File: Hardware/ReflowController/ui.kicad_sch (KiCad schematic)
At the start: 46 parts, among them J601 LCD_HEADER, Q601 BC848, SW601 RotaryEncoder_Switch, SW602 SW_UP, SW603 SW_DOWN, SW604 SW_LEFT, SW605 SW_RIGHT, SW606 SW_SELECT, SW607 SW_RET, SW608 SW_RESET, U601 PI4IOE5V6416

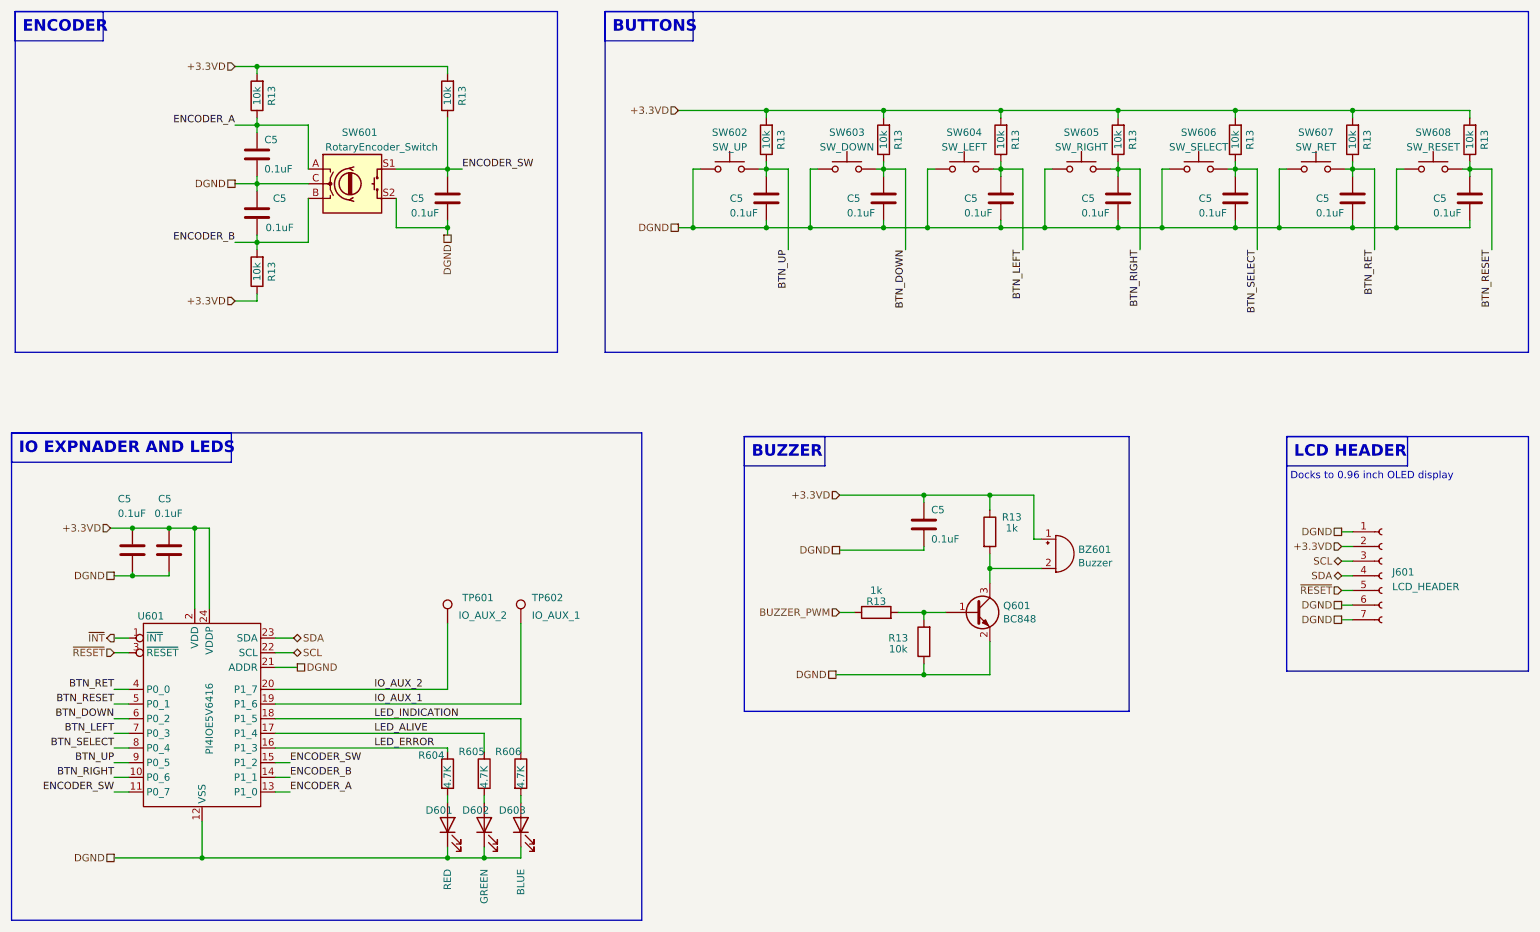
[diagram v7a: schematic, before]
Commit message: Advancing on the pcb removed netties from MCU
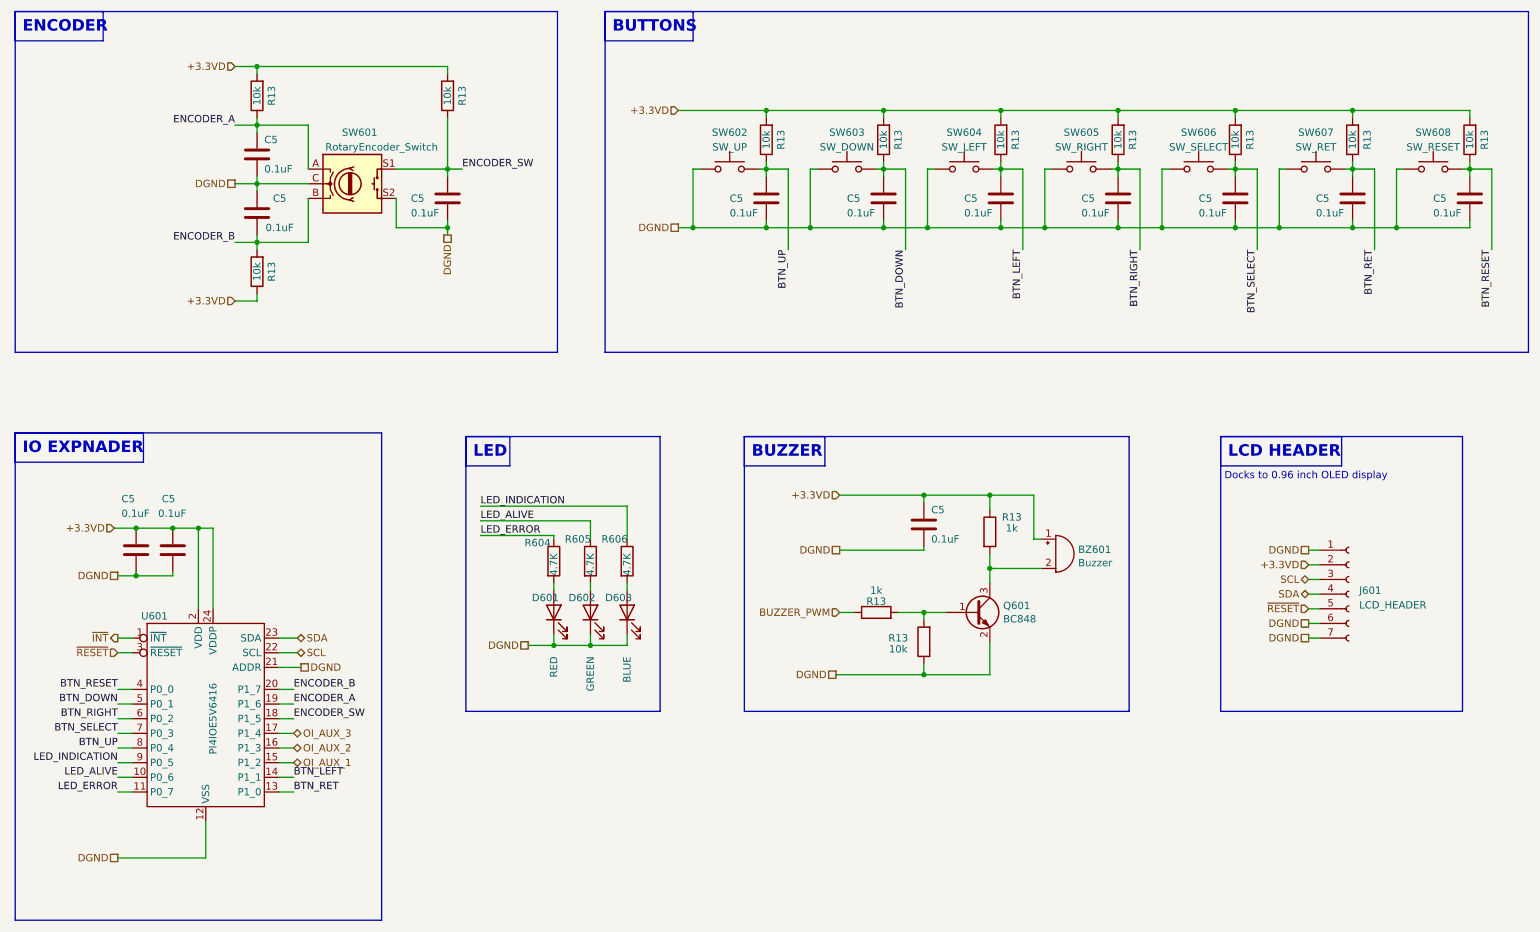
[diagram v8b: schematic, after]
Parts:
- removed TP601: IO_AUX_2, TestPoint:TestPoint_Pad_D1.5mm, symbol Connector:TestPoint
- removed TP602: IO_AUX_1, TestPoint:TestPoint_Pad_D1.5mm, symbol Connector:TestPoint
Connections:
- net IO_AUX_1 is gone; now on net ENCODER_A: U601.19 (P1_6)
- net IO_AUX_2 is gone; now on net ENCODER_B: U601.20 (P1_7)
- net BTN_DOWN: now also U601.5 (P0_1); no longer U601.6 (P0_2)
- net BTN_LEFT: now also U601.14 (P1_1); no longer U601.7 (P0_3)
- net BTN_RESET: now also U601.4 (P0_0); no longer U601.5 (P0_1)
- net BTN_RET: now also U601.13 (P1_0); no longer U601.4 (P0_0)
- net BTN_RIGHT: now also U601.6 (P0_2); no longer U601.10 (P0_6)
- net BTN_SELECT: now also U601.7 (P0_3); no longer U601.8 (P0_4)
- net BTN_UP: now also U601.8 (P0_4); no longer U601.9 (P0_5)
- net ENCODER_A: no longer U601.13 (P1_0)
- net ENCODER_B: no longer U601.14 (P1_1)
- net ENCODER_SW: now also U601.18 (P1_5); no longer U601.11 (P0_7), U601.15 (P1_2)
- net LED_ALIVE: now also U601.10 (P0_6); no longer U601.17 (P1_4)
- net LED_ERROR: now also U601.11 (P0_7); no longer U601.16 (P1_3)
- net LED_INDICATION: now also U601.9 (P0_5); no longer U601.18 (P1_5)
- new net OI_AUX_1: U601.15 (P1_2)
- new net OI_AUX_2: U601.16 (P1_3)
- new net OI_AUX_3: U601.17 (P1_4)
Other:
- note added: "IO EXPNADER"
- note added: "LED"
- note removed: "IO EXPNADER AND LEDS"
- moved on the sheet: C5, D601, D602, D603, J601, R604, R605, R606, U601
